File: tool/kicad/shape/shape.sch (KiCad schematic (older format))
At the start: 91 parts, among them J1 MICRO-USB-AB, K1 CONN_3, P10 TEST_POINT, P27 TEST_POINT, P28 TEST_POINT, P29 TEST_POINT, P30 CONN_3X2, P31 CONN_7, P35 CONN_6, P37 TEST_POINT, P38 TEST_POINT, P5 CONN_6, U1 SN74LVC2T45, U2 ST-USBLC6-2, U3 EFM32GG332, U4 YM2413, X1 48Mhz, X2 CRYSTAL

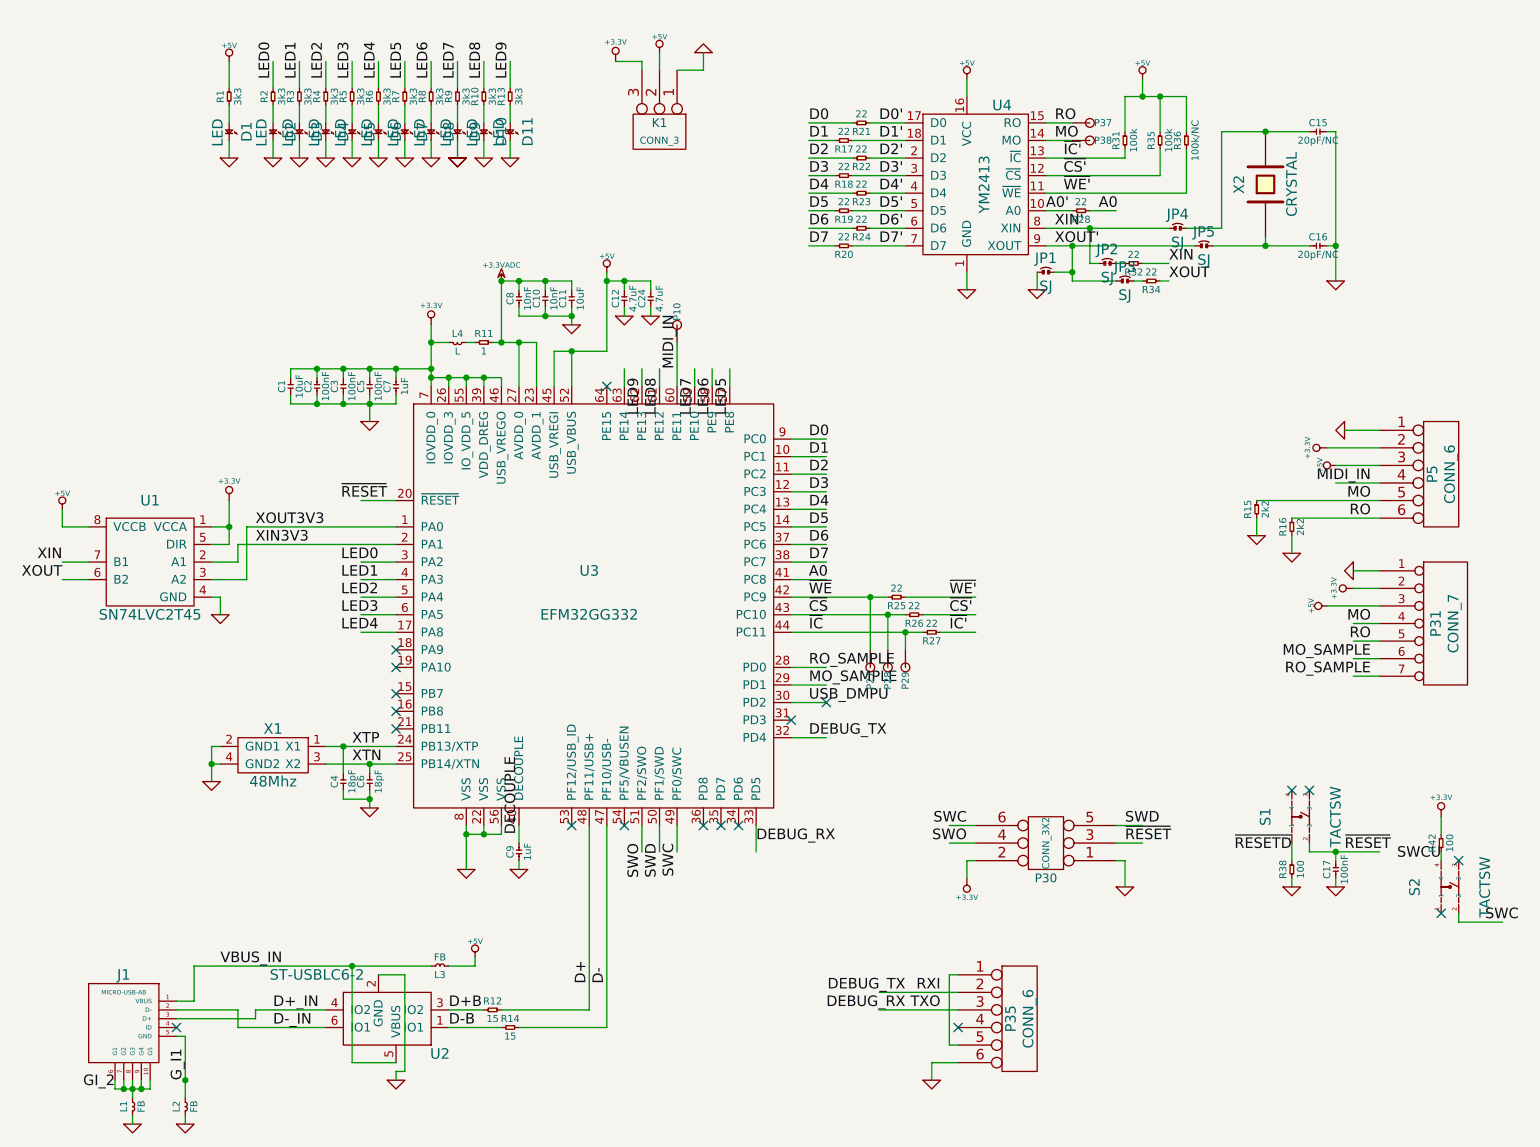
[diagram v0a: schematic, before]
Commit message: add opamp spec, cleanup shape board
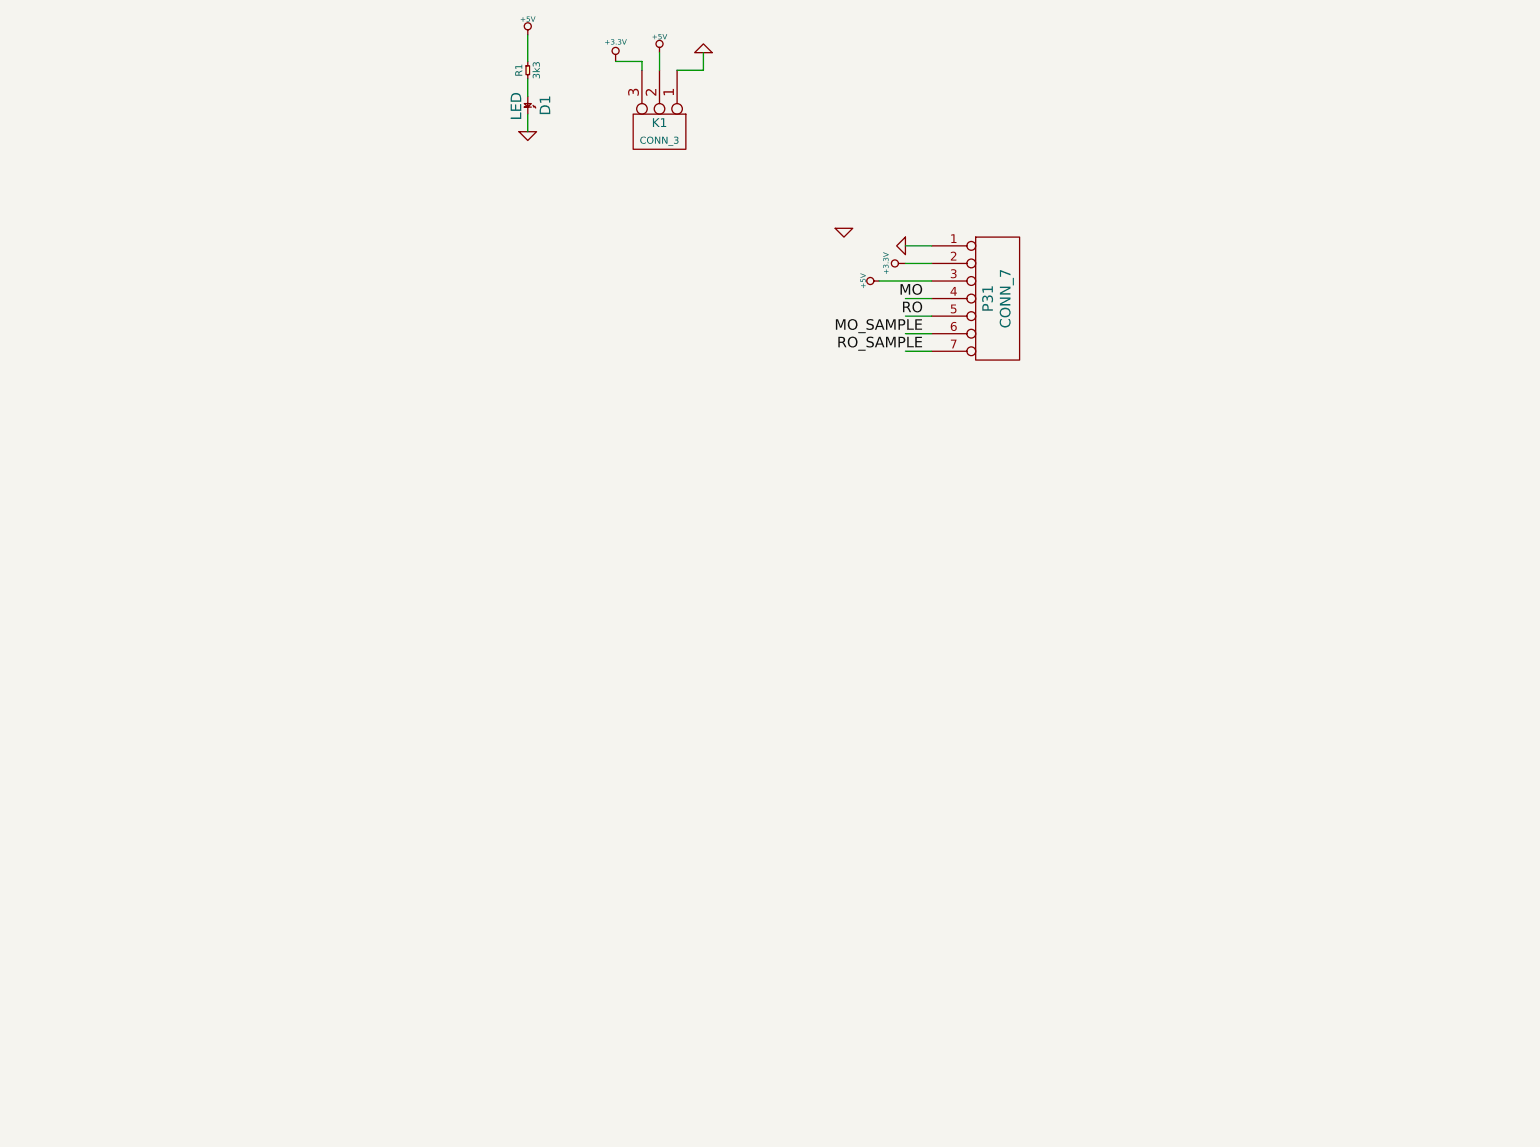
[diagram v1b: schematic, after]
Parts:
- removed C1, C11: 10uF, symbol C
- removed C10, C8: 10nF, symbol C
- removed C12, C24: 4.7uF, symbol C
- removed C15, C16: 20pF/NC, symbol C
- removed C17, C2, C3, C5: 100nF, symbol C
- removed C4, C6: 18pF, symbol C
- removed C7, C9: 1uF, symbol C
- removed D10, D11, D2, D3, D4, D5, D6, D7, D8, D9: LED, symbol LED
- removed J1: MICRO-USB-AB, symbol MICRO-USB-AB
- removed JP1, JP2, JP3, JP4, JP5: SJ, symbol SJ
- removed L1, L2, L3: FB, symbol L
- removed L4: L, symbol L
- removed P10, P27, P28, P29, P37, P38: TEST_POINT, symbol TEST_POINT
- removed P30: CONN_3X2, symbol CONN_3X2
- removed P35, P5: CONN_6, symbol CONN_6
- removed R10, R13, R2, R3, R4, R5, R6, R7, R8, R9: 3k3, symbol R
- removed R11: 1, symbol R
- removed R12, R14: 15, symbol R
- removed R15, R16: 2k2, symbol R
- removed R17, R18, R19, R20, R21, R22, R23, R24, R25, R26, R27, R28, R32, R34: 22, symbol R
- removed R31, R35: 100k, symbol R
- removed R36: 100k/NC, symbol R
- removed R38, R42: 100, symbol R
- removed S1, S2: TACTSW, symbol TACTSW
- removed U1: SN74LVC2T45, symbol SN74LVC2T45
- removed U2: ST-USBLC6-2, symbol ST-USBLC6-2
- removed U3: EFM32GG332, symbol EFM32GG332
- removed U4: YM2413, symbol YM2413
- removed X1: 48Mhz, symbol TXC-XTAL
- removed X2: CRYSTAL, symbol CRYSTAL
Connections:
- net labels removed: +3.3VADC, A0, A0', D+, D+B, D+_IN, D-, D-B, D-_IN, D0, D0', D1, D1', D2, D2', D3, D3', D4, D4', D5, D5', D6, D6', D7, D7', DEBUG_RX, DEBUG_TX, DECOUPLE, GI_2, G_I1, LED0, LED1, LED2, LED3, LED4, LED5, LED6, LED7, LED8, LED9, MIDI_IN, RXI, SWC, SWCU, SWD, SWO, TXO, USB_DMPU, VBUS_IN, XIN, XIN', XIN3V3, XOUT, XOUT', XOUT3V3, XTN, XTP, ~CS, ~CS', ~IC, ~IC', ~RESET, ~RESETD, ~WE, ~WE'
- wire segments 275 -> 15
- no-connect marks 19 -> 0
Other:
- moved on the sheet: D1, P31, R1

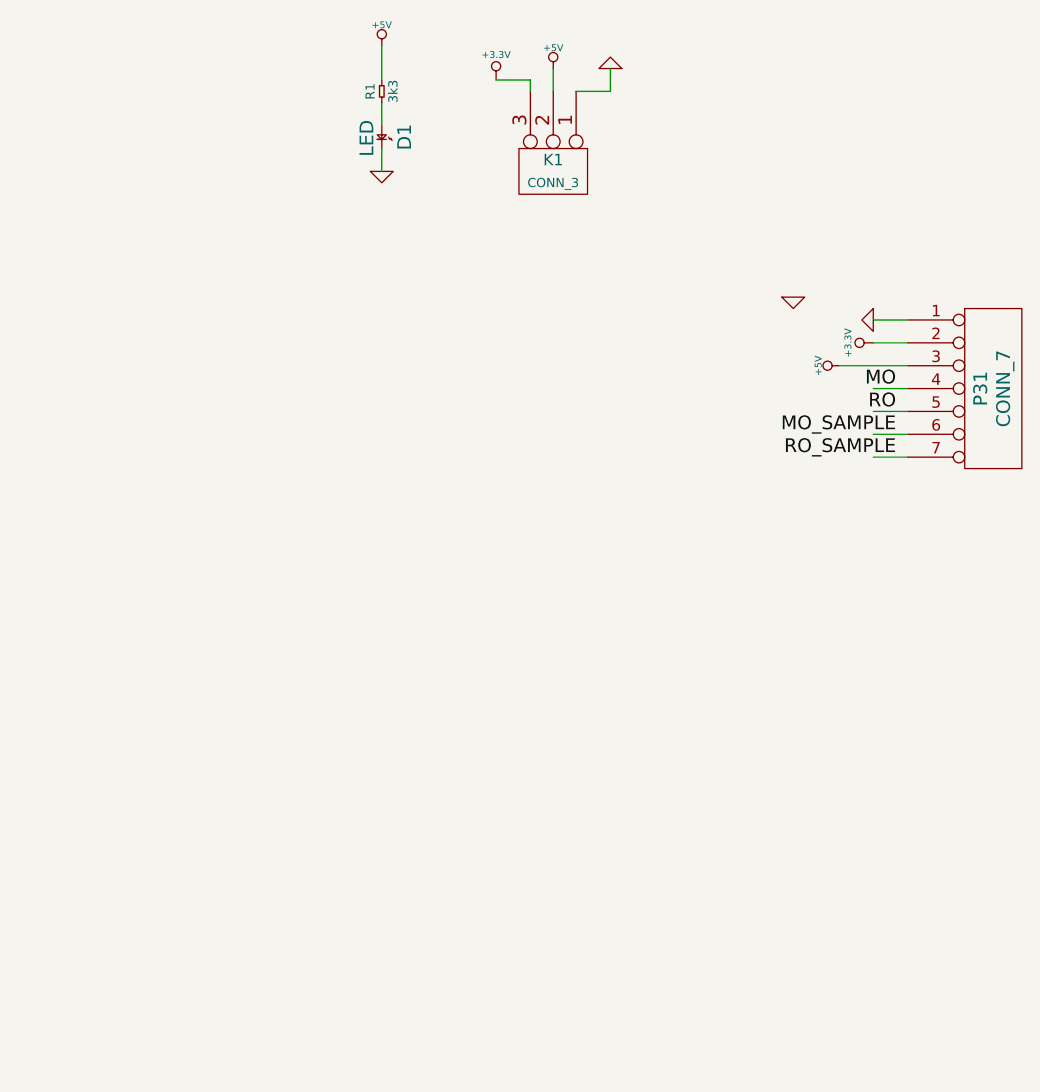
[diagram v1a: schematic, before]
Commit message: shape board schematic
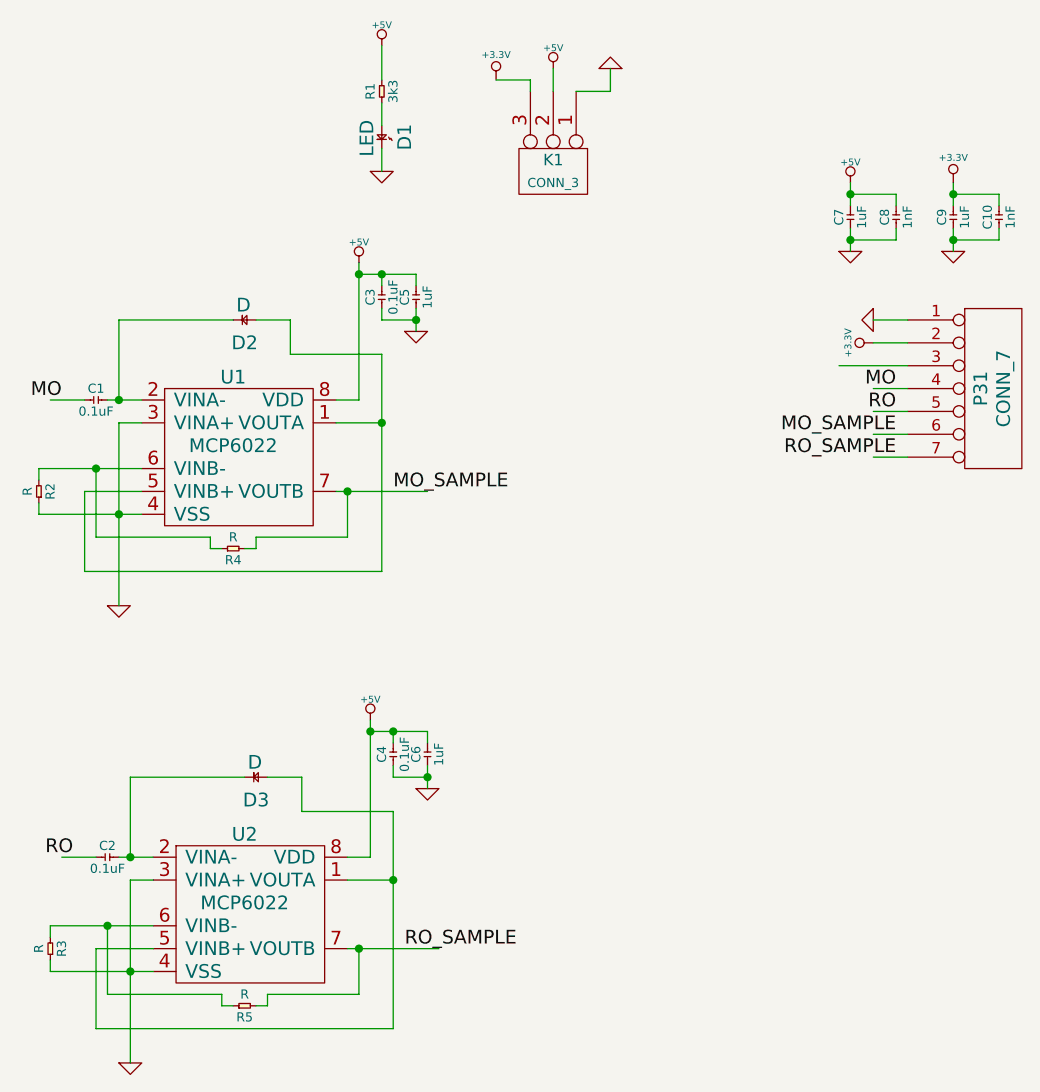
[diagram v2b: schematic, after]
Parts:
- added C1, C2, C3, C4: 0.1uF, symbol C
- added C10, C8: 1nF, symbol C
- added C5, C6, C7, C9: 1uF, symbol C
- added D2, D3: D, symbol D
- added R2, R3, R4, R5: R, symbol R
- added U1, U2: MCP6022, symbol MCP6022
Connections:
- wire segments 15 -> 97

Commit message: rough layout
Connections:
- net labels added: MOA, MOO, ROA, ROO
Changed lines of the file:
@@
 	1    0    0    -1
 $EndComp
+$Comp
+L +5V #PWR018
+U 1 1 53DE12BC
+P 5600 2500
+F 0 "#PWR018" H 5600 2590 20  0001 C CNN
+F 1 "+5V" H 5600 2590 30  0000 C CNN
+F 2 "" H 5600 2500 60  0000 C CNN
+F 3 "" H 5600 2500 60  0000 C CNN
+	1    5600 2500
+	0    -1   -1   0
+$EndComp
+Text Label 2450 2500 0    60   ~ 0
+MOA
+Text Label 2500 4450 0    60   ~ 0
+ROA
+Text Label 3600 2650 0    60   ~ 0
+MOO
+Text Label 3650 4600 0    60   ~ 0
+ROO
 $EndSCHEMATC

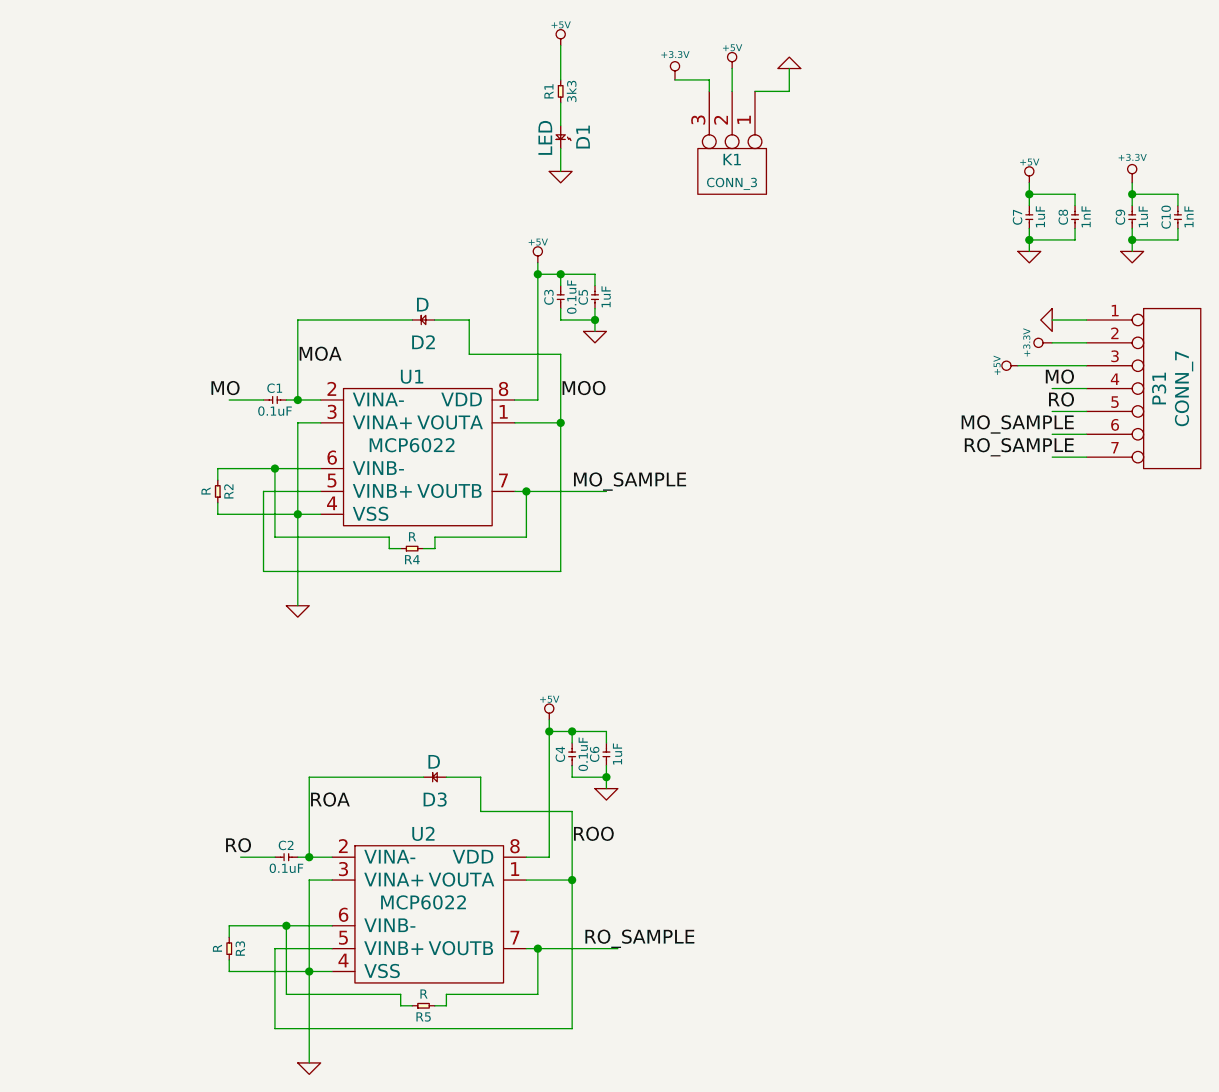
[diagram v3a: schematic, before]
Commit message: updated shaper board design (tested in breadboard)
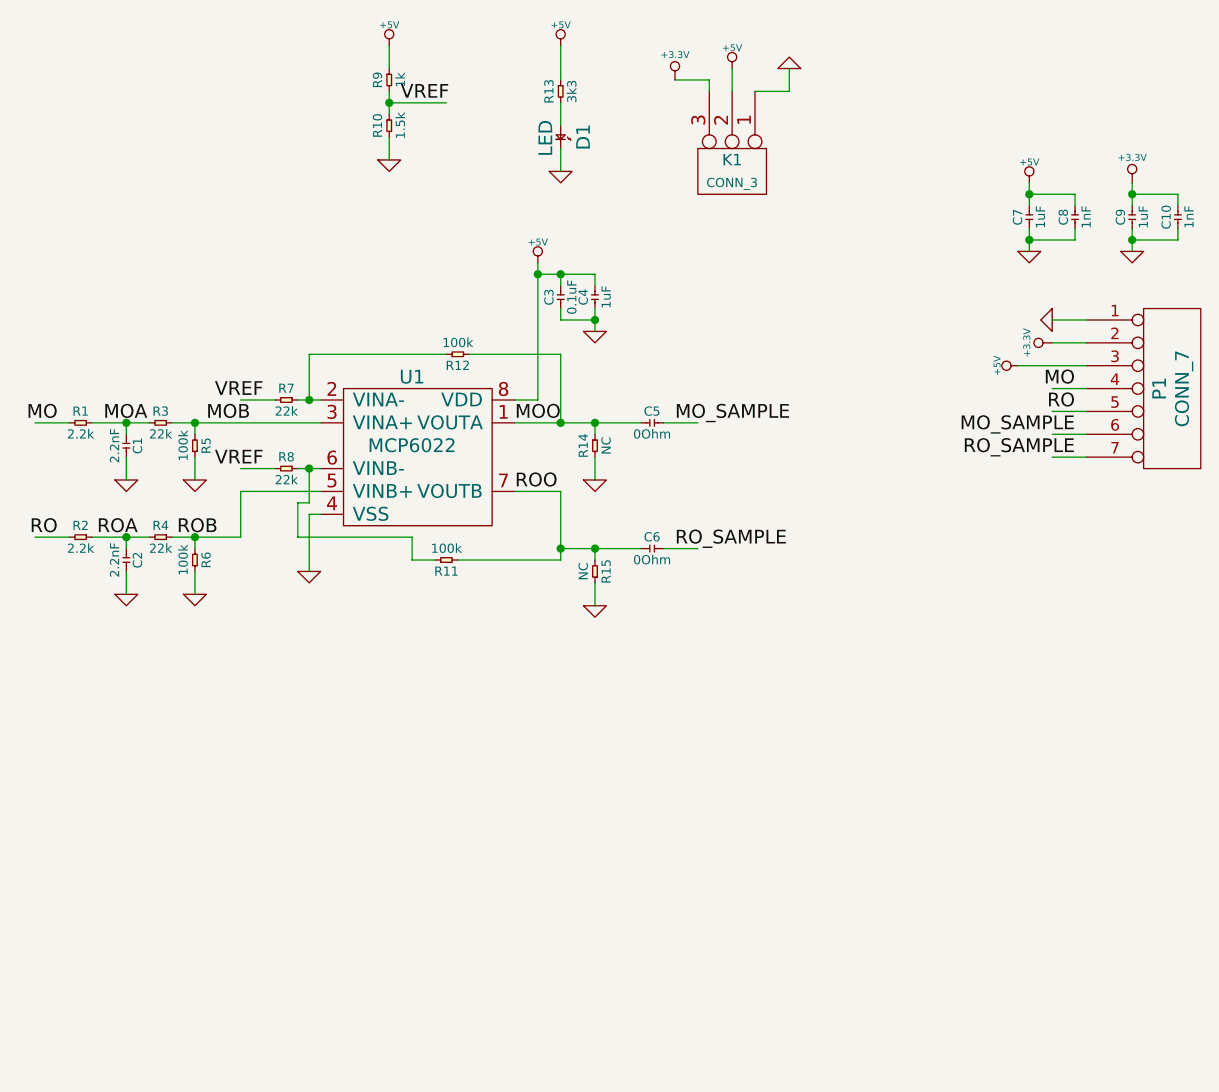
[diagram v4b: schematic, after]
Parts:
- removed C4: 0.1uF, symbol C
- removed D2, D3: D, symbol D
- removed U2: MCP6022, symbol MCP6022
- added C5: 0Ohm, symbol C
- added R1: 2.2k, symbol R
- added R10: 1.5k, symbol R
- added R11, R12, R6: 100k, symbol R
- added R14, R15: NC, symbol R
- added R7, R8: 22k, symbol R
- added R9: 1k, symbol R
- C1, C2: value 0.1uF -> 2.2nF
- C6: value 1uF -> 0Ohm
- R2: value R -> 2.2k
- R3, R4: value R -> 22k
- R5: value R -> 100k
- renumbered C5 to C4, P31 to P1, R1 to R13
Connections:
- net labels added: MOB, ROB, VREF
- wire segments 97 -> 82

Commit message: add board.hh
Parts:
- R3, R4, R7, R8: value 22k -> 33k
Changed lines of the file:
@@
 LIBS:valves
 LIBS:shape-cache
-EELAYER 24 0
+EELAYER 25 0
 EELAYER END
 $Descr A4 11693 8268
@@
 P 2400 2650
 F 0 "R7" H 2400 2700 40  0000 C CNN
-F 1 "22k" H 2400 2600 40  0000 C CNN
+F 1 "33k" H 2400 2600 40  0000 C CNN
 F 2 "" H 2400 2650 60  0000 C CNN
 F 3 "" H 2400 2650 60  0000 C CNN
@@
 P 1850 2750
 F 0 "R3" H 1850 2800 40  0000 C CNN
-F 1 "22k" H 1850 2700 40  0000 C CNN
+F 1 "33k" H 1850 2700 40  0000 C CNN
 F 2 "" H 1850 2750 60  0000 C CNN
 F 3 "" H 1850 2750 60  0000 C CNN
@@
 P 2400 2950
 F 0 "R8" H 2400 3000 40  0000 C CNN
-F 1 "22k" H 2400 2900 40  0000 C CNN
+F 1 "33k" H 2400 2900 40  0000 C CNN
 F 2 "" H 2400 2950 60  0000 C CNN
 F 3 "" H 2400 2950 60  0000 C CNN
@@
 P 1850 3250
 F 0 "R4" H 1850 3300 40  0000 C CNN
-F 1 "22k" H 1850 3200 40  0000 C CNN
+F 1 "33k" H 1850 3200 40  0000 C CNN
 F 2 "" H 1850 3250 60  0000 C CNN
 F 3 "" H 1850 3250 60  0000 C CNN
